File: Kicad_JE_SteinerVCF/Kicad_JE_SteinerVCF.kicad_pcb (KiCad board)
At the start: 2 copper layers, 100 x 100 mm, 98 parts, among them J101 HP, J102 BP, J103 LP, J104 Out, J105 CV, J201 HP, J202 BP, J203 LP, J204 Out, J205 CV, P101 Doepfer_Power_10pin, P201 Doepfer_Power_10pin, Q101 BC559, Q102 BC549, Q103 BC549, Q104 BC549, Q201 MMBT2907A, Q202 MMBT2222A, Q203 MMBT2222A, Q204 MMBT2222A

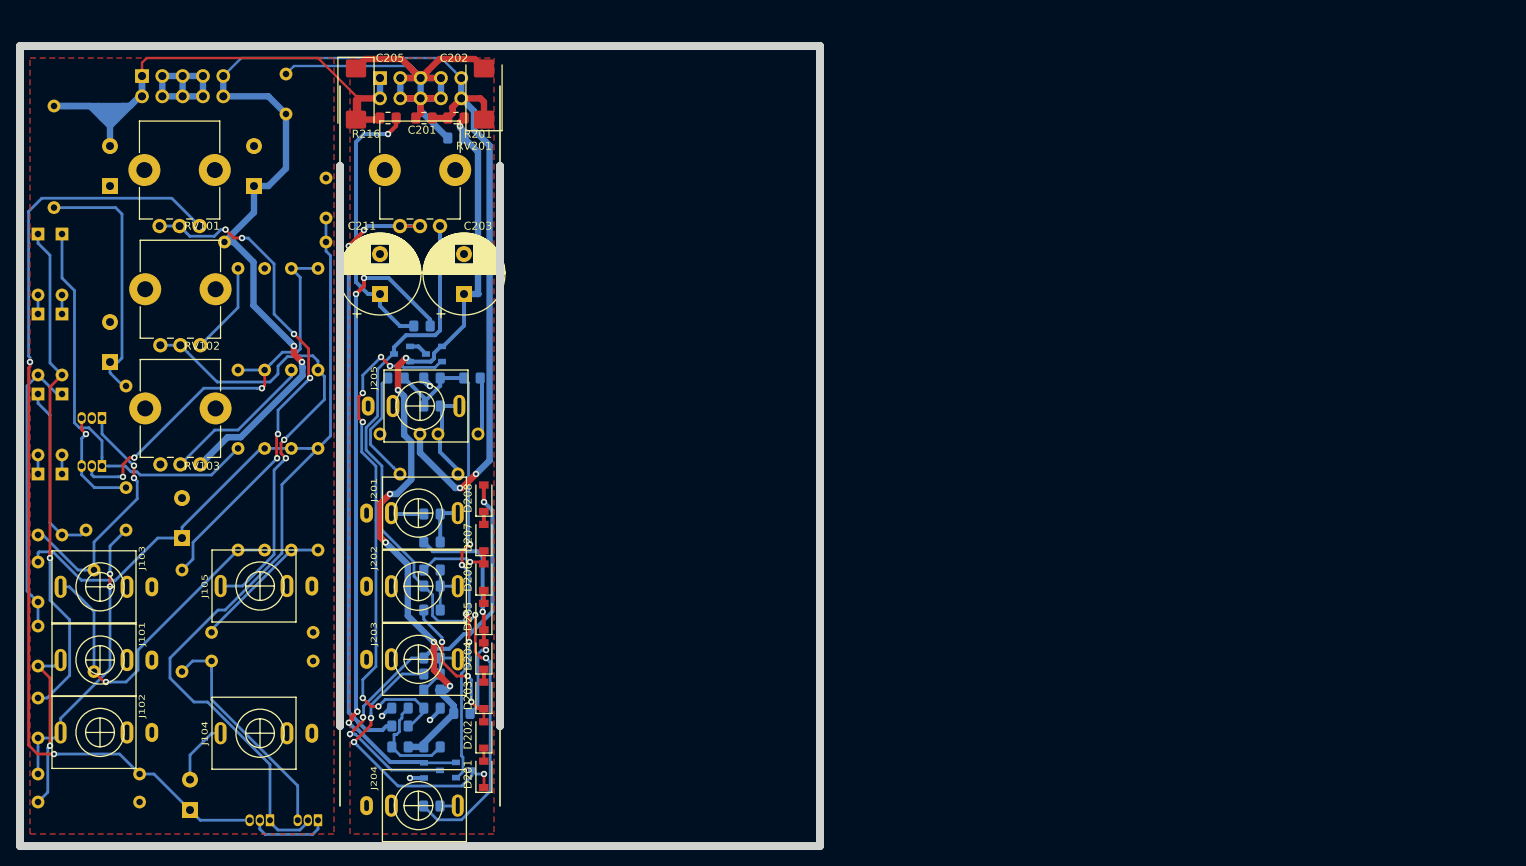
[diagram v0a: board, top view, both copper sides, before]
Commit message: VCO ICL8083 netlist and PCB import
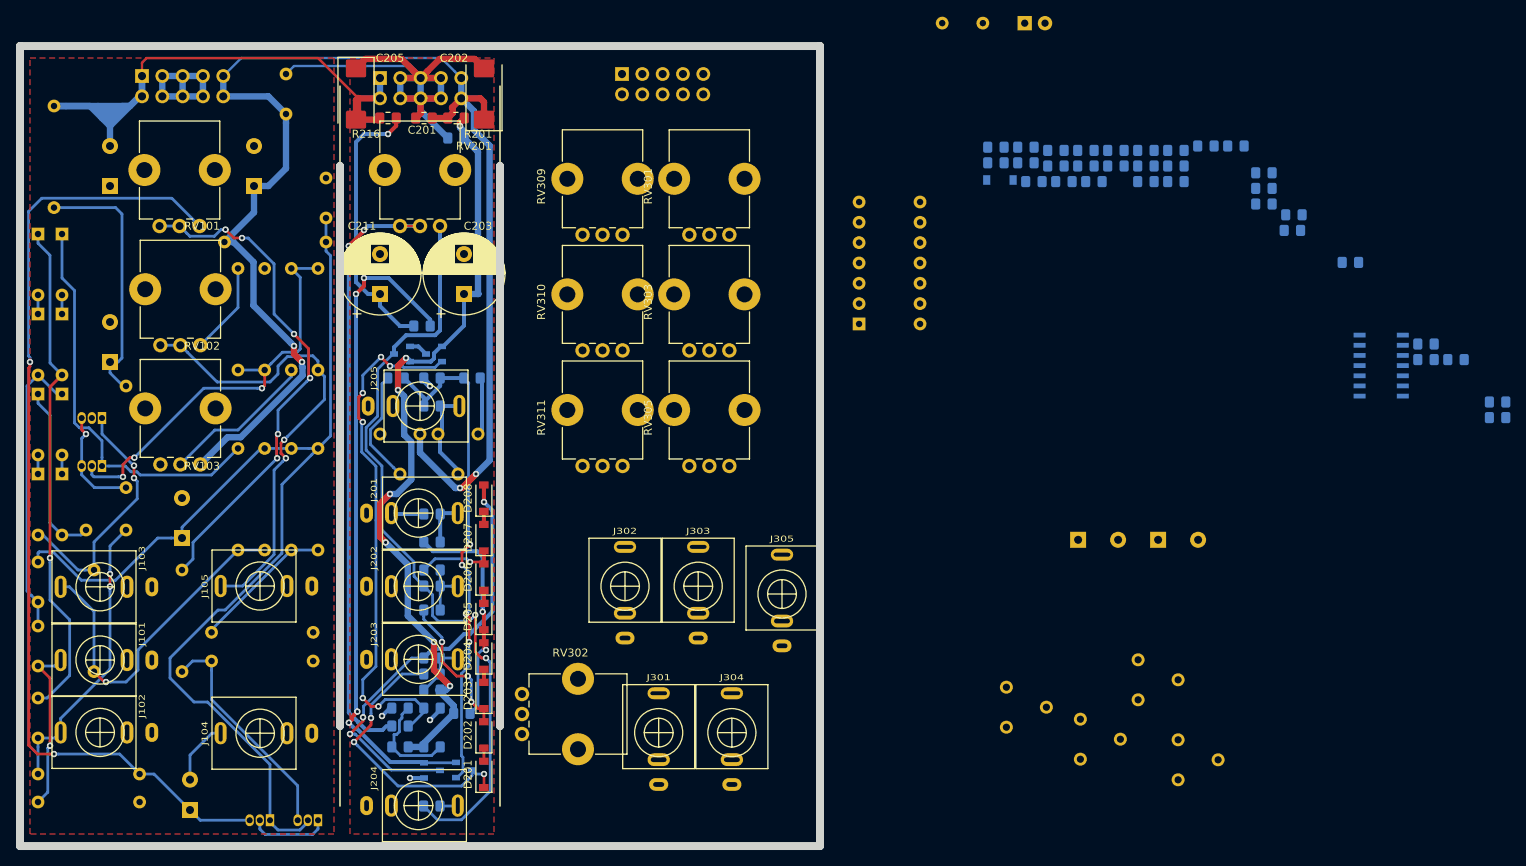
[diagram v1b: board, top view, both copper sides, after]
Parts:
- added C301: 100n, Capacitor_SMD:C_0805_2012Metric_Pad1.15x1.40mm_HandSolder, B.Cu at (180.5, 66.9)
- added C302: 100u, Capacitor_THT:CP_Radial_D10.0mm_P5.00mm, B.Cu at (182.3, 111.7)
- added C303: 100n, Capacitor_SMD:C_0805_2012Metric_Pad1.15x1.40mm_HandSolder, B.Cu at (225.7, 87.2)
- added C304: 100u, Capacitor_THT:CP_Radial_D10.0mm_P5.00mm, B.Cu at (192.3, 111.7)
- added C305: 4n7, Capacitor_SMD:C_0805_2012Metric_Pad1.15x1.40mm_HandSolder, B.Cu at (202.0, 62.5)
- added C306: 4u7, Capacitor_SMD:C_0805_2012Metric_Pad1.15x1.40mm_HandSolder, B.Cu at (209.2, 71.1)
- added C307: 1n, Capacitor_SMD:C_0805_2012Metric_Pad1.15x1.40mm_HandSolder, B.Cu at (234.7, 96.4)
- added D301: LED, LED_THT:LED_D5.0mm, B.Cu at (175.6, 47.1)
- added D302: MMSD4148, Diode_SMD:D_SOD-123, B.Cu at (172.5, 66.7)
- added J301: Sine, AJ-Dropbox-Kicad:PJ301SM, F.Cu at (129.8, 135.8)
- added J302: Tri, AJ-Dropbox-Kicad:PJ301SM, F.Cu at (125.6, 117.5)
- added J303: Sq, AJ-Dropbox-Kicad:PJ301SM, F.Cu at (134.8, 117.5)
- added J304: CV, AJ-Dropbox-Kicad:PJ301SM, F.Cu at (139.0, 135.8)
- added J305: CV, AJ-Dropbox-Kicad:PJ301SM, F.Cu at (145.2, 118.5)
- added P301: Doepfer_Power_10pin, Connectors_IDC:IDC-Header_2x05_Pitch2.54mm_Straight, B.Cu at (125.2, 53.5)
- added R301: 5k6, Resistor_SMD:R_0805_2012Metric_Pad1.15x1.40mm_HandSolder, B.Cu at (176.7, 66.9)
- added R302: 24k, Resistor_SMD:R_0805_2012Metric_Pad1.15x1.40mm_HandSolder, B.Cu at (190.7, 65.0)
- added R303: 12k, Resistor_SMD:R_0805_2012Metric_Pad1.15x1.40mm_HandSolder, B.Cu at (194.5, 66.9)
- added R304: 10k, Resistor_SMD:R_0805_2012Metric_Pad1.15x1.40mm_HandSolder, B.Cu at (190.7, 66.9)
- added R305: 120k, Resistor_SMD:R_0805_2012Metric_Pad1.15x1.40mm_HandSolder, B.Cu at (187.0, 65.0)
- added R306: 30k, Resistor_SMD:R_0805_2012Metric_Pad1.15x1.40mm_HandSolder, B.Cu at (183.2, 63.0)
- added R307: 0R, Resistor_SMD:R_0805_2012Metric_Pad1.15x1.40mm_HandSolder, B.Cu at (179.5, 63.0)
- added R308: 0R, Resistor_SMD:R_0805_2012Metric_Pad1.15x1.40mm_HandSolder, B.Cu at (183.2, 65.0)
- added R309: 10k, Resistor_SMD:R_0805_2012Metric_Pad1.15x1.40mm_HandSolder, B.Cu at (184.2, 66.9)
- added R310: 24k, Resistor_SMD:R_0805_2012Metric_Pad1.15x1.40mm_HandSolder, B.Cu at (179.5, 65.0)
- added R311: 10k, Resistor_SMD:R_0805_2012Metric_Pad1.15x1.40mm_HandSolder, B.Cu at (175.7, 62.6)
- added R312: 1k5, Resistor_SMD:R_0805_2012Metric_Pad1.15x1.40mm_HandSolder, B.Cu at (172.0, 62.6)
- added R313: 1k5, Resistor_SMD:R_0805_2012Metric_Pad1.15x1.40mm_HandSolder, B.Cu at (172.0, 64.6)
- added R314: 470k, Resistor_SMD:R_0805_2012Metric_Pad1.15x1.40mm_HandSolder, B.Cu at (229.5, 89.2)
- added R315: 0R, Resistor_SMD:R_0805_2012Metric_Pad1.15x1.40mm_HandSolder, B.Cu at (190.7, 63.0)
- added R316: 12k, Resistor_SMD:R_0805_2012Metric_Pad1.15x1.40mm_HandSolder, B.Cu at (194.5, 65.0)
- added R317: 0R, Resistor_SMD:R_0805_2012Metric_Pad1.15x1.40mm_HandSolder, B.Cu at (194.5, 63.0)
- added R318: 0R, Resistor_SMD:R_0805_2012Metric_Pad1.15x1.40mm_HandSolder, B.Cu at (209.0, 73.0)
- added R319: LDR03, OptoDevice:R_LDR_7x6mm_P5.1mm_Vertical, B.Cu at (165.3, 47.1)
- added R320: 470k, Resistor_SMD:R_0805_2012Metric_Pad1.15x1.40mm_HandSolder, B.Cu at (205.5, 69.7)
- added R321: 470k, Resistor_SMD:R_0805_2012Metric_Pad1.15x1.40mm_HandSolder, B.Cu at (198.2, 62.5)
- added R322: 10k, Resistor_SMD:R_0805_2012Metric_Pad1.15x1.40mm_HandSolder, B.Cu at (225.7, 89.2)
- added R323: 10M, Resistor_SMD:R_0805_2012Metric_Pad1.15x1.40mm_HandSolder, B.Cu at (205.5, 67.8)
- added R324: 470k, Resistor_SMD:R_0805_2012Metric_Pad1.15x1.40mm_HandSolder, B.Cu at (187.0, 63.0)
- added R325: 100k, Resistor_SMD:R_0805_2012Metric_Pad1.15x1.40mm_HandSolder, B.Cu at (216.3, 77.0)
- added R326: 100k, Resistor_SMD:R_0805_2012Metric_Pad1.15x1.40mm_HandSolder, B.Cu at (234.7, 94.5)
- added R327: 10M, Resistor_SMD:R_0805_2012Metric_Pad1.15x1.40mm_HandSolder, B.Cu at (205.5, 65.8)
- added R328: 0R, Resistor_SMD:R_0805_2012Metric_Pad1.15x1.40mm_HandSolder, B.Cu at (175.7, 64.6)
- added RV301: 10k, Potentiometer_THT:Potentiometer_Alps_RK09K_Single_Vertical, F.Cu at (138.7, 73.6)
- added RV302: 10k, Potentiometer_THT:Potentiometer_Alps_RK09K_Single_Vertical, F.Cu at (112.8, 136.0)
- added RV303: 100k, Potentiometer_THT:Potentiometer_Alps_RK09K_Single_Vertical, F.Cu at (138.7, 88.0)
- added RV304: 1k, Potentiometer_THT:Potentiometer_Piher_PT-6-V_Vertical, B.Cu at (173.3, 130.1)
- added RV305: 10k, Potentiometer_THT:Potentiometer_Alps_RK09K_Single_Vertical, F.Cu at (138.7, 102.5)
- added RV306: 100k, Potentiometer_THT:Potentiometer_Piher_PT-6-V_Vertical, B.Cu at (189.8, 126.7)
- added RV307: 10k, Potentiometer_THT:Potentiometer_Piher_PT-6-V_Vertical, B.Cu at (194.8, 136.7)
- added RV308: 100k, Potentiometer_THT:Potentiometer_Piher_PT-6-V_Vertical, B.Cu at (182.5, 134.1)
- added RV309: 100k, Potentiometer_THT:Potentiometer_Alps_RK09K_Single_Vertical, F.Cu at (125.3, 73.6)
- added RV310: 100k, Potentiometer_THT:Potentiometer_Alps_RK09K_Single_Vertical, F.Cu at (125.3, 88.0)
- added RV311: 100k, Potentiometer_THT:Potentiometer_Alps_RK09K_Single_Vertical, F.Cu at (125.3, 102.5)
- added U301: TL074, Package_SO:SOIC-14_3.9x8.7mm_P1.27mm, B.Cu at (220.1, 89.9)
- added U302: ICL8038, Package_DIP:DIP-14_W7.62mm, B.Cu at (154.9, 84.7)

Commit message: Components for faceplate mounted
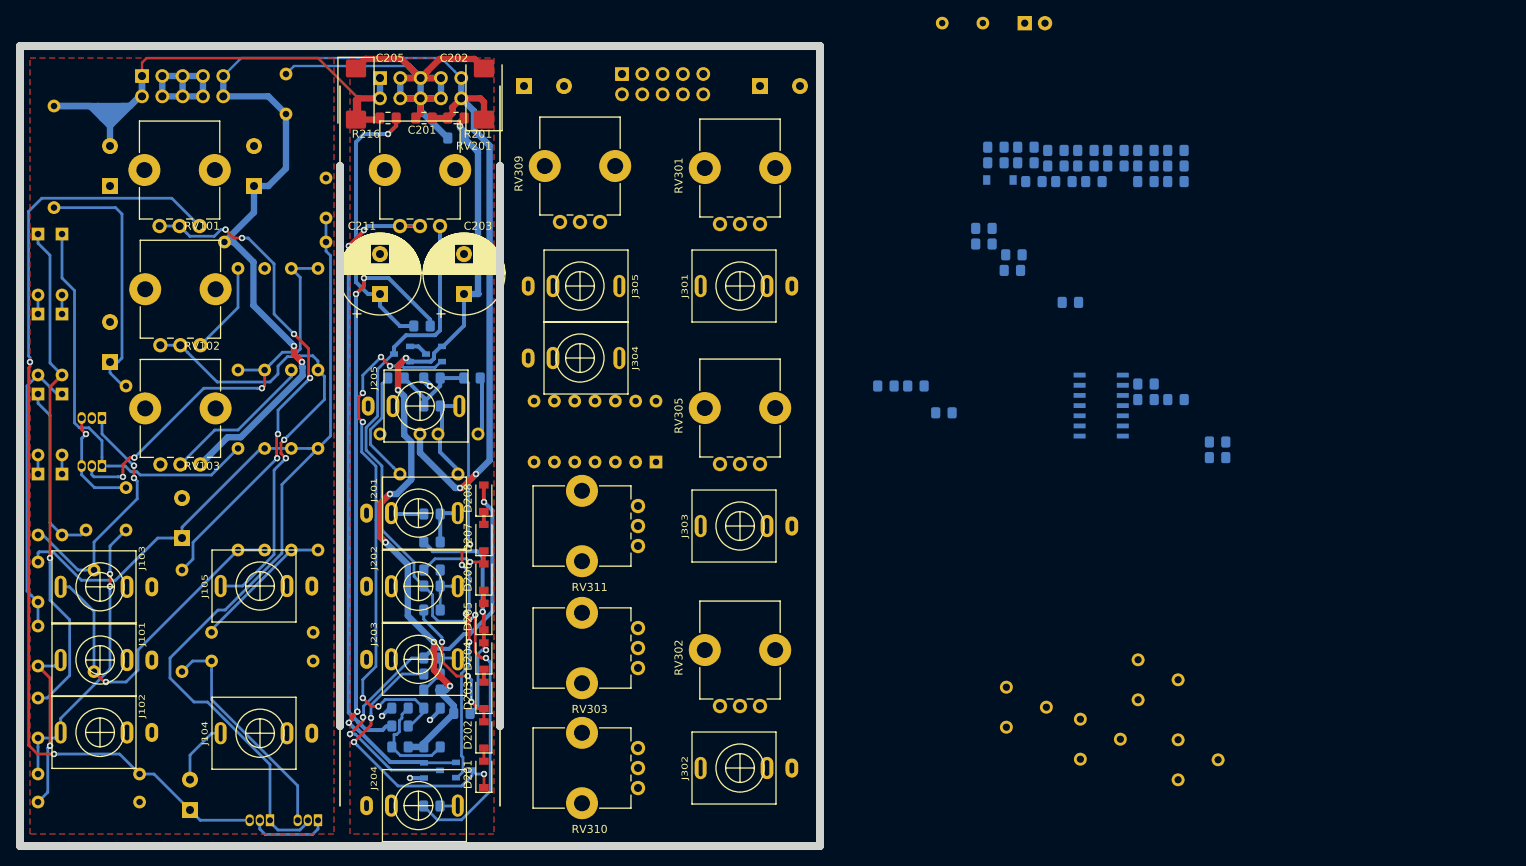
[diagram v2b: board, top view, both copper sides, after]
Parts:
- RV301: value 10k -> 10k Sin
- RV302: value 10k -> 10k Tri
- RV303: value 100k -> 100k Duty
- RV305: value 10k -> 10k SQ
- RV309: value 100k -> 100k CV
- RV310: value 100k -> 100k Coarse
- RV311: value 100k -> 100k fine
- moved C304 97.5 mm to (113.0, 55.0)
- moved C302 69.3 mm to (142.5, 55.0)
- moved J301 56.7 mm to (140.0, 80.0), turned to 90 degrees
- moved J304 50.5 mm to (120.0, 89.0), turned to 270 degrees
- moved C305 50.0 mm to (162.0, 92.5)
- moved R321 50.0 mm to (158.2, 92.5)
- moved R327 50.0 mm to (165.5, 95.8)
- moved RV310 49.7 mm to (127.2, 137.8), turned to 180 degrees
- moved J305 46.0 mm to (120.0, 80.0), turned to 270 degrees
- moved RV303 36.5 mm to (127.2, 122.8), turned to 180 degrees
- moved C303 35.4 mm to (190.7, 92.2)
- moved C306 35.4 mm to (174.2, 76.1)
- moved C307 35.4 mm to (199.7, 101.4)
- moved R314 35.4 mm to (194.5, 94.2)
- moved R318 35.4 mm to (174.0, 78.0)
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
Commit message: PCB - Components placed on VCO
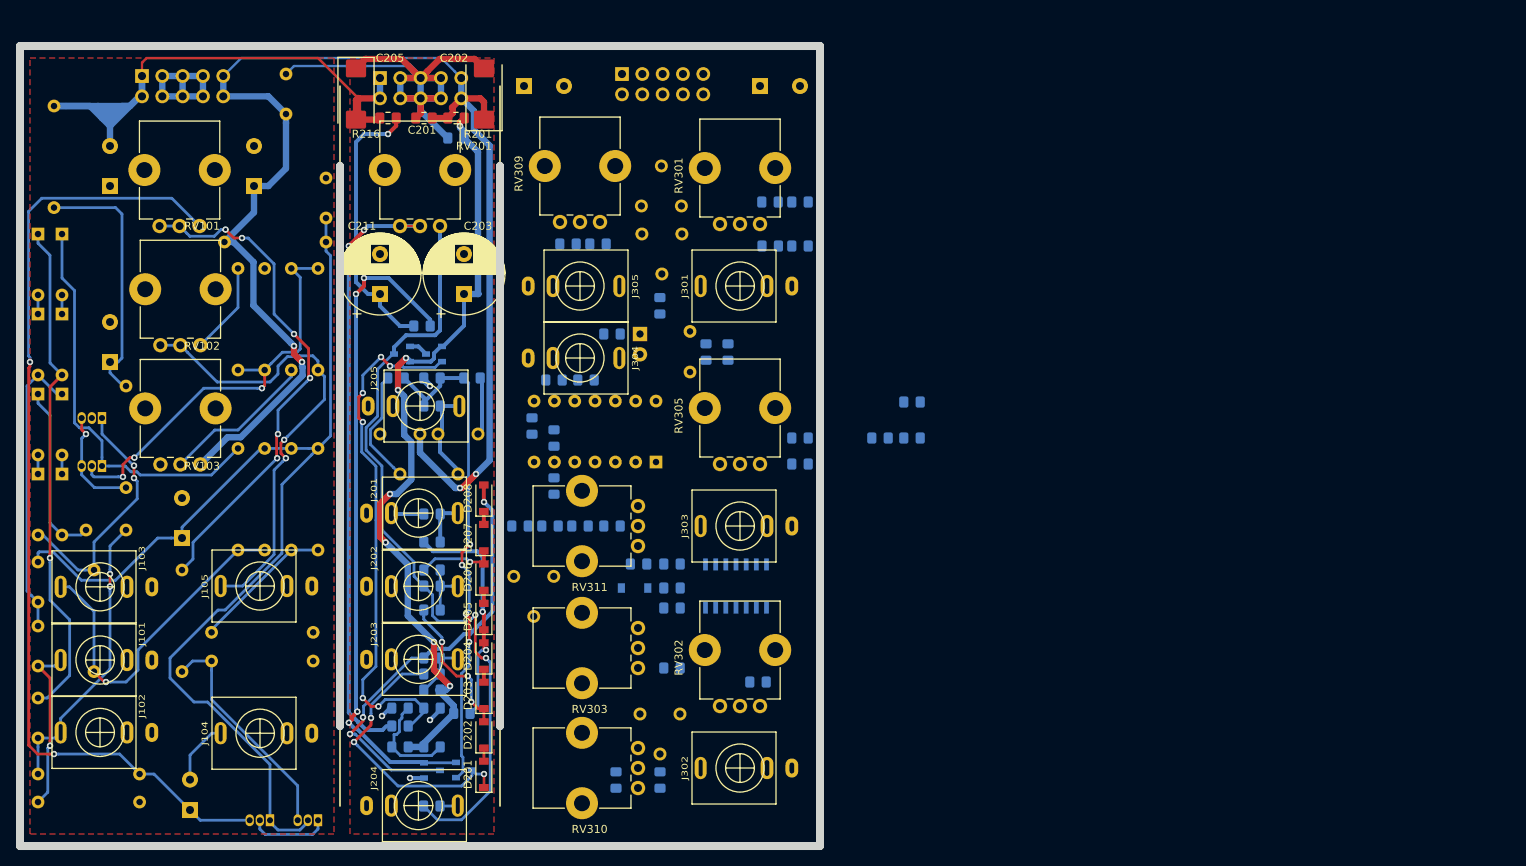
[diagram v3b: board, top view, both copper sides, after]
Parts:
- moved RV307 94.6 mm to (127.7, 70.0), turned to 90 degrees
- moved R326 86.3 mm to (124.5, 141.8), turned to 90 degrees
- moved R317 85.6 mm to (116.8, 99.0), turned to 90 degrees
- moved R315 85.1 mm to (116.8, 105.0), turned to 270 degrees
- moved R316 82.2 mm to (116.8, 91.8), turned to 180 degrees
- moved R309 80.5 mm to (131.5, 127.8)
- moved C307 80.2 mm to (120.0, 110.0)
- moved R323 80.0 mm to (130.0, 141.8), turned to 270 degrees
- moved RV306 78.0 mm to (132.7, 73.5), turned to 270 degrees
- moved R305 77.7 mm to (127.3, 114.8), turned to 180 degrees
- moved R302 77.4 mm to (131.5, 114.8), turned to 180 degrees
- moved R308 76.4 mm to (142.2, 129.5)
- moved R312 76.0 mm to (112.5, 110.0), turned to 180 degrees
- moved R306 75.3 mm to (131.5, 117.8), turned to 180 degrees
- moved R313 71.9 mm to (116.2, 110.0), turned to 180 degrees
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
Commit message: All routed - And 3D
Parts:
- C306: moved to F.Cu
- moved C306 41.0 mm to (120.5, 96.5)
- moved C303 31.9 mm to (131.8, 110.5)
- moved C301 20.5 mm to (143.8, 83.8), turned to 180 degrees
- moved R305 11.4 mm to (135.2, 106.5)
- moved RV307 8.70 mm to (132.5, 62.8), turned to 270 degrees
- moved R306 6.21 mm to (135.5, 113.0), turned to 0 degrees
- moved R315 2.14 mm to (114.8, 105.8)
- moved R302 1.77 mm to (131.8, 113.0), turned to 0 degrees
- moved U301 0.90 mm to (140.0, 118.2)
- turned R318 to 270 degrees
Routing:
- net +12VA: track 176.0 -> 367.3 mm, vias 4 -> 12
- net -12VA: track 88.6 -> 263.6 mm, vias 0 -> 1
- net Net-(C307-Pad2): track 0.00 -> 141.6 mm, vias 0 -> 4
- net Net-(R312-Pad1): track 0.00 -> 74.2 mm, vias 0 -> 4
- net Net-(C307-Pad1): track 0.00 -> 69.5 mm, vias 0 -> 4
- net Net-(R310-Pad2): track 0.00 -> 66.2 mm, vias 0 -> 8
- net Net-(R301-Pad2): track 0.00 -> 58.0 mm
- net Net-(RV303-Pad2): track 0.00 -> 51.6 mm, vias 0 -> 1
- net Net-(R304-Pad1): track 0.00 -> 51.2 mm, vias 0 -> 2
- net GNDA: track 102.4 -> 145.9 mm, vias 4 -> 10
- net Net-(R313-Pad1): track 0.00 -> 43.5 mm, vias 0 -> 3
- net Net-(R322-Pad1): track 0.00 -> 30.5 mm
- net Net-(R311-Pad1): track 0.00 -> 29.5 mm, vias 0 -> 3
- net Net-(R306-Pad1): track 0.00 -> 28.3 mm, vias 0 -> 4
- net Net-(U301-Pad3): track 0.00 -> 28.2 mm, vias 0 -> 2
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
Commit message: Gerber and DRC
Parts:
- J302: value Tri -> Triangle
- J303: value Sq -> Square
- J304: value CV -> CV Vactrol
- RV101: value 1k -> 1k - Adj Q
- RV102: value 500k -> 500k CV Lin
- RV103: value 25k -> 25k Freq
- RV201: value 1k -> 1k Q-Adj
- RV202 1V/Oct: renamed from RV202
- RV203 Freq: renamed from RV203
- RV302: value 10k Tri -> 10k Triangle
- RV304: value 1k -> 1k Symetry
- RV306: value 100k -> 100k LF Sym
- RV307: value 10k -> 10k Max Trim
- RV308: value 100k -> 100k min trim
- renumbered D301 to LED301
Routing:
- net -12VA: track 263.6 -> 319.9 mm
- net +12VA: track 367.3 -> 399.3 mm, vias 12 -> 13
- net GNDA: track 145.9 -> 153.2 mm
- net (no net): track 2.54 -> 0.00 mm
- net Net-(R327-Pad2): track 0.00 -> 2.22 mm
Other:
- board text added: "Johansen Engineering VCF 1974 - 2019W04"
- board text added: "Johansen Engineering VCO 8083 - 2019W04"
- board text added: "VC0"
- board text added: "VC0 8083"
- board text added: "VCF"
- board text added: "VCO"
